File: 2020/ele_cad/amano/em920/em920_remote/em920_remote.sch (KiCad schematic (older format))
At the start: 11 parts, among them SW1 SW_Push, SW2 SW_SPST, U1 ATtiny85-20PU, U2 TY92SS, U3 AE-XCL102D333CR-G

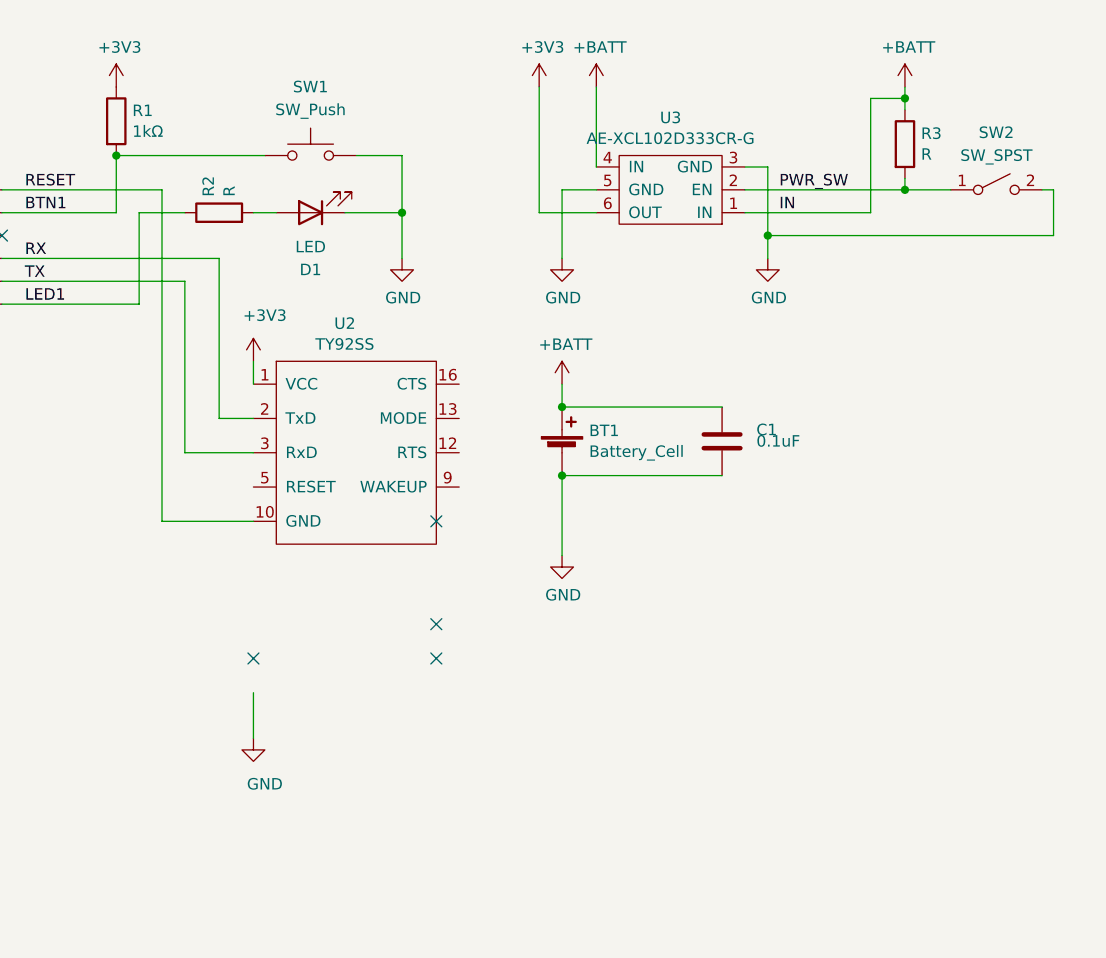
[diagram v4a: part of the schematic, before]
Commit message: リモコンのDCDCを昇降圧に変更
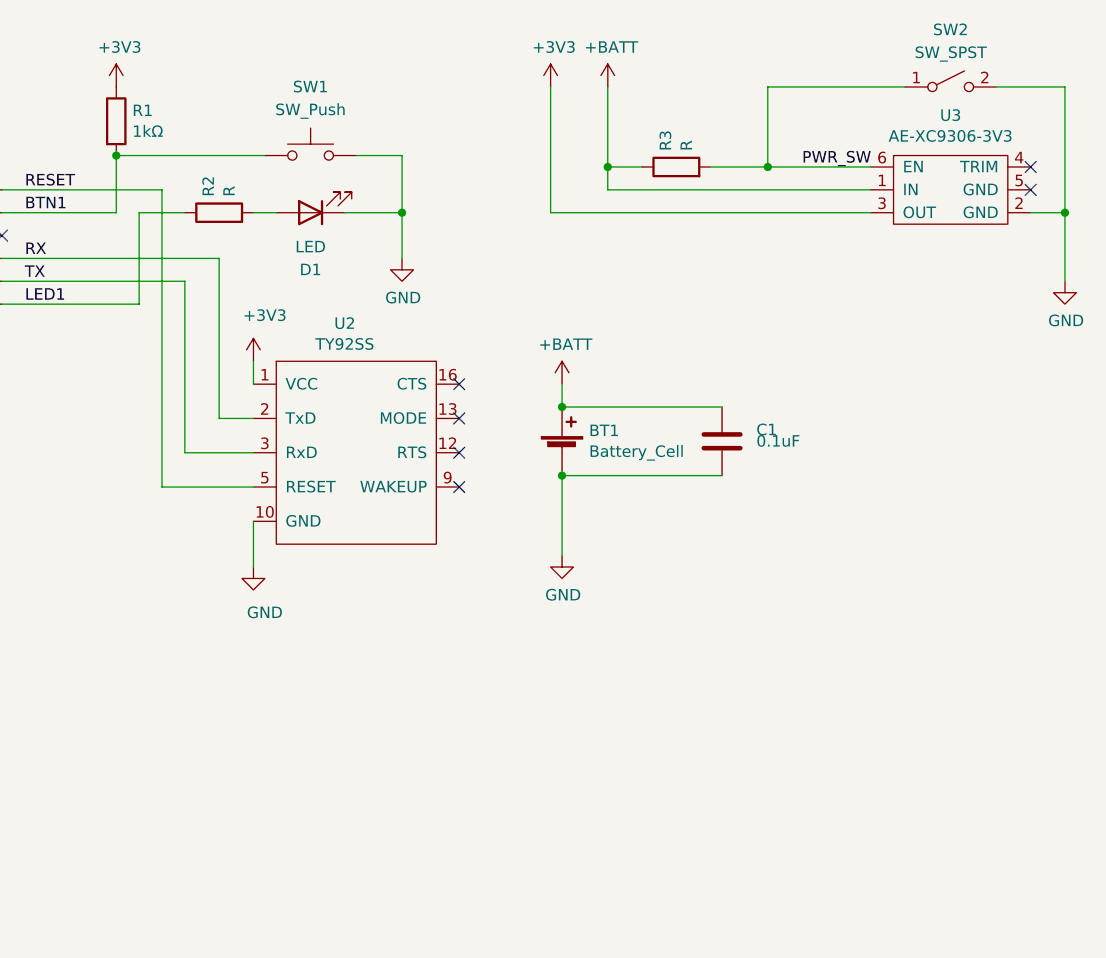
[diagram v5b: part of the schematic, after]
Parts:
- removed U3: AE-XCL102D333CR-G, em920:AE-XCL102D333CR-G, symbol em920:AE-XCL102D333CR-G
- added U3: AE-XC9306-3V3, em920:AE-XC9306-3V3, symbol em920:AE-XC9306-3V3
- BT1: footprint Battery:BatteryHolder_Keystone_103_1x20mm -> Connector_PinHeader_2.54mm:PinHeader_1x03_P2.54mm_Vertical
- R1, R2, R3: footprint Resistor_THT:R_Axial_DIN0207_L6.3mm_D2.5mm_P2.54mm_Vertical -> Resistor_THT:R_Axial_DIN0207_L6.3mm_D2.5mm_P7.62mm_Horizontal
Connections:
- net +3V3: now also U3.3 (OUT)
- net +BATT: now also U3.1 (IN)
- net GND: now also U2.10 (GND), U3.2 (GND)
- net PWR_SW: now also U3.6 (EN)
- net RESET: now also U2.5 (RESET); no longer U2.10 (GND)
- no-connect marks 6 -> 8
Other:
- moved on the sheet: R3, SW2
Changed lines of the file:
@@
 L power:GND #PWR04
 U 1 1 60FD4012
-P 5400 5950
-F 0 "#PWR04" H 5400 5700 50  0001 C CNN
-F 1 "GND" H 5450 5750 50  0000 C CNN
-F 2 "" H 5400 5950 50  0001 C CNN
-F 3 "" H 5400 5950 50  0001 C CNN
-	1    5400 5950
-	1    0    0    -1
-$EndComp
-Wire Wire Line
-	5400 5750 5400 5950
-Wire Wire Line
-	5000 5000 5400 5000
+P 5400 5200
+F 0 "#PWR04" H 5400 4950 50  0001 C CNN
+F 1 "GND" H 5450 5000 50  0000 C CNN
+F 2 "" H 5400 5200 50  0001 C CNN
+F 3 "" H 5400 5200 50  0001 C CNN
+	1    5400 5200
+	1    0    0    -1
+$EndComp
+Wire Wire Line
+	5400 5000 5400 5200
+Wire Wire Line
+	5000 4850 5400 4850
 Text Label 4400 3550 0    50   ~ 0
 RESET
 Wire Wire Line
 	4300 3950 5100 3950
-NoConn ~ 6200 5000
-NoConn ~ 6200 5450
-NoConn ~ 6200 5600
-NoConn ~ 5400 5600
 NoConn ~ 2750 2850
 $Comp
@@
 F 0 "BT1" H 6868 4796 50  0000 L CNN
 F 1 "Battery_Cell" H 6868 4705 50  0000 L CNN
-F 2 "Battery:BatteryHolder_Keystone_103_1x20mm" V 6750 4760 50  0001 C CNN
+F 2 "Connector_PinHeader_2.54mm:PinHeader_1x03_P2.54mm_Vertical" V 6750 4760 50  0001 C CNN
 F 3 "~" V 6750 4760 50  0001 C CNN
 	1    6750 4700
@@
 F 0 "R2" H 5320 3696 50  0000 L CNN
 F 1 "R" H 5320 3605 50  0000 L CNN
-F 2 "Resistor_THT:R_Axial_DIN0207_L6.3mm_D2.5mm_P2.54mm_Vertical" V 5180 3650 50  0001 C CNN
+F 2 "Resistor_THT:R_Axial_DIN0207_L6.3mm_D2.5mm_P7.62mm_Horizontal" V 5180 3650 50  0001 C CNN
 F 3 "~" H 5250 3650 50  0001 C CNN
 	1    5250 3650
@@
 F 0 "R1" H 4870 3296 50  0000 L CNN
 F 1 "1kΩ" H 4870 3205 50  0000 L CNN
-F 2 "Resistor_THT:R_Axial_DIN0207_L6.3mm_D2.5mm_P2.54mm_Vertical" V 4730 3250 50  0001 C CNN
+F 2 "Resistor_THT:R_Axial_DIN0207_L6.3mm_D2.5mm_P7.62mm_Horizontal" V 4730 3250 50  0001 C CNN
 F 3 "~" H 4800 3250 50  0001 C CNN
 	1    4800 3250
@@
 	4300 3550 5000 3550
 Wire Wire Line
-	5000 3550 5000 5000
+	5000 3550 5000 4850
 Wire Wire Line
 	5400 3650 5500 3650
@@
 	4900 3650 5100 3650
 $Comp
-L power:GND #PWR011
-U 1 1 61018775
-P 6750 3850
-F 0 "#PWR011" H 6750 3600 50  0001 C CNN
-F 1 "GND" H 6755 3677 50  0000 C CNN
-F 2 "" H 6750 3850 50  0001 C CNN
-F 3 "" H 6750 3850 50  0001 C CNN
-	1    6750 3850
-	1    0    0    -1
-$EndComp
-$Comp
 L power:+3V3 #PWR012
 U 1 1 6101B33D
-P 6650 3100
-F 0 "#PWR012" H 6650 2950 50  0001 C CNN
-F 1 "+3V3" H 6665 3273 50  0000 C CNN
-F 2 "" H 6650 3100 50  0001 C CNN
-F 3 "" H 6650 3100 50  0001 C CNN
-	1    6650 3100
+P 6700 3100
+F 0 "#PWR012" H 6700 2950 50  0001 C CNN
+F 1 "+3V3" H 6715 3273 50  0000 C CNN
+F 2 "" H 6700 3100 50  0001 C CNN
+F 3 "" H 6700 3100 50  0001 C CNN
+	1    6700 3100
 	1    0    0    -1
 $EndComp
@@
 $EndComp
 $Comp
-L em920:AE-XCL102D333CR-G U3
-U 1 1 6105883F
-P 7550 3450
-F 0 "U3" H 7875 3235 50  0000 C CNN
-F 1 "AE-XCL102D333CR-G" H 7875 3326 50  0000 C CNN
-F 2 "em920:AE-XCL102D333CR-G" H 7850 3750 50  0001 C CNN
-F 3 "" H 7850 3750 50  0001 C CNN
-	1    7550 3450
-	-1   0    0    1
-$EndComp
-Wire Wire Line
-	6900 3100 6900 3450
-$Comp
 L power:+BATT #PWR09
 U 1 1 6101B870
-P 6900 3100
-F 0 "#PWR09" H 6900 2950 50  0001 C CNN
-F 1 "+BATT" H 6915 3273 50  0000 C CNN
-F 2 "" H 6900 3100 50  0001 C CNN
-F 3 "" H 6900 3100 50  0001 C CNN
-	1    6900 3100
-	1    0    0    -1
-$EndComp
-Wire Wire Line
-	6900 3550 6750 3550
-Wire Wire Line
-	6650 3650 6650 3100
-$Comp
-L Switch:SW_SPST SW2
-U 1 1 610E4997
-P 8650 3550
-F 0 "SW2" H 8650 3800 50  0000 C CNN
-F 1 "SW_SPST" H 8650 3700 50  0000 C CNN
-F 2 "em920:SlideSW" H 8650 3550 50  0001 C CNN
-F 3 "~" H 8650 3550 50  0001 C CNN
-	1    8650 3550
-	1    0    0    -1
-$EndComp
-$Comp
-L Device:R R3
-U 1 1 610E7CBC
-P 8250 3350
-F 0 "R3" H 8320 3396 50  0000 L CNN
-F 1 "R" H 8320 3305 50  0000 L CNN
-F 2 "Resistor_THT:R_Axial_DIN0207_L6.3mm_D2.5mm_P2.54mm_Vertical" V 8180 3350 50  0001 C CNN
-F 3 "~" H 8250 3350 50  0001 C CNN
-	1    8250 3350
-	1    0    0    -1
-$EndComp
-$Comp
-L power:+BATT #PWR014
-U 1 1 610EDAF3
-P 8250 3100
-F 0 "#PWR014" H 8250 2950 50  0001 C CNN
-F 1 "+BATT" H 8265 3273 50  0000 C CNN
-F 2 "" H 8250 3100 50  0001 C CNN
-F 3 "" H 8250 3100 50  0001 C CNN
-	1    8250 3100
-	1    0    0    -1
-$EndComp
-Wire Wire Line
-	6750 3550 6750 3850
-$Comp
-L power:GND #PWR013
-U 1 1 610F5EE2
-P 7650 3850
-F 0 "#PWR013" H 7650 3600 50  0001 C CNN
-F 1 "GND" H 7655 3677 50  0000 C CNN
-F 2 "" H 7650 3850 50  0001 C CNN
-F 3 "" H 7650 3850 50  0001 C CNN
-	1    7650 3850
-	1    0    0    -1
-$EndComp
-Wire Wire Line
-	7550 3450 7650 3450
-Wire Wire Line
-	7650 3450 7650 3750
+P 6950 3100
+F 0 "#PWR09" H 6950 2950 50  0001 C CNN
+F 1 "+BATT" H 6965 3273 50  0000 C CNN
+F 2 "" H 6950 3100 50  0001 C CNN
+F 3 "" H 6950 3100 50  0001 C CNN
+	1    6950 3100
+	1    0    0    -1
+$EndComp
+Wire Wire Line
+	6700 3650 6700 3100
 $Comp
 L power:+BATT #PWR0102
@@
 	-1   0    0    1
 $EndComp
-Wire Wire Line
-	6650 3650 6900 3650
-Wire Wire Line
-	7550 3550 8250 3550
-Wire Wire Line
-	8250 3500 8250 3550
-Connection ~ 8250 3550
-Wire Wire Line
-	8250 3100 8250 3150
-Wire Wire Line
-	7550 3650 8100 3650
-Wire Wire Line
-	8100 3650 8100 3150
-Wire Wire Line
-	8100 3150 8250 3150
-Connection ~ 8250 3150
-Wire Wire Line
-	8250 3150 8250 3200
-Connection ~ 7650 3750
-Wire Wire Line
-	7650 3750 7650 3850
-Wire Wire Line
-	8250 3550 8450 3550
-Wire Wire Line
-	8850 3550 8900 3550
-Wire Wire Line
-	8900 3550 8900 3750
-Wire Wire Line
-	7650 3750 8900 3750
-Text Label 7700 3550 0    50   ~ 0
+NoConn ~ 6300 4400
+NoConn ~ 6300 4550
+NoConn ~ 6300 4700
+NoConn ~ 6300 4850
+$Comp
+L Device:R R3
+U 1 1 610E7CBC
+P 7250 3450
+F 0 "R3" H 7320 3496 50  0000 L CNN
+F 1 "R" H 7320 3405 50  0000 L CNN
+F 2 "Resistor_THT:R_Axial_DIN0207_L6.3mm_D2.5mm_P7.62mm_Horizontal" V 7180 3450 50  0001 C CNN
+F 3 "~" H 7250 3450 50  0001 C CNN
+	1    7250 3450
+	0    -1   -1   0
+$EndComp
+Wire Wire Line
+	6950 3100 6950 3450
+$Comp
+L Switch:SW_SPST SW2
+U 1 1 610E4997
+P 8450 3100
+F 0 "SW2" H 8450 3350 50  0000 C CNN
+F 1 "SW_SPST" H 8450 3250 50  0000 C CNN
+F 2 "em920:SlideSW" H 8450 3100 50  0001 C CNN
+F 3 "~" H 8450 3100 50  0001 C CNN
+	1    8450 3100
+	1    0    0    -1
+$EndComp
+$Comp
+L power:GND #PWR011
+U 1 1 61018775
+P 8950 3950
+F 0 "#PWR011" H 8950 3700 50  0001 C CNN
+F 1 "GND" H 8955 3777 50  0000 C CNN
+F 2 "" H 8950 3950 50  0001 C CNN
+F 3 "" H 8950 3950 50  0001 C CNN
+	1    8950 3950
+	1    0    0    -1
+$EndComp
+$Comp
+L em920:AE-XC9306-3V3 U3
+U 1 1 6117DFD8
+P 8450 3350
+F 0 "U3" H 8450 3475 50  0000 C CNN
+F 1 "AE-XC9306-3V3" H 8450 3384 50  0000 C CNN
+F 2 "em920:AE-XC9306-3V3" H 8200 3350 50  0001 C CNN
+F 3 "" H 8200 3350 50  0001 C CNN
+	1    8450 3350
+	1    0    0    -1
+$EndComp
+Wire Wire Line
+	6700 3650 8100 3650
+Wire Wire Line
+	8100 3550 6950 3550
+Text Label 7800 3450 0    50   ~ 0
 PWR_SW
-Text Label 7700 3650 0    50   ~ 0
-IN
+Wire Wire Line
+	7400 3450 7650 3450
+Wire Wire Line
+	7100 3450 6950 3450
+Connection ~ 6950 3450
+Wire Wire Line
+	6950 3450 6950 3550
+Wire Wire Line
+	7650 3450 7650 3100
+Wire Wire Line
+	7650 3100 8250 3100
+Connection ~ 7650 3450
+Wire Wire Line
+	7650 3450 8100 3450
+Wire Wire Line
+	8650 3100 8950 3100
+Wire Wire Line
+	8950 3100 8950 3650
+Wire Wire Line
+	8800 3650 8950 3650
+Connection ~ 8950 3650
+Wire Wire Line
+	8950 3650 8950 3950
+NoConn ~ 8800 3550
+NoConn ~ 8800 3450
 $EndSCHEMATC

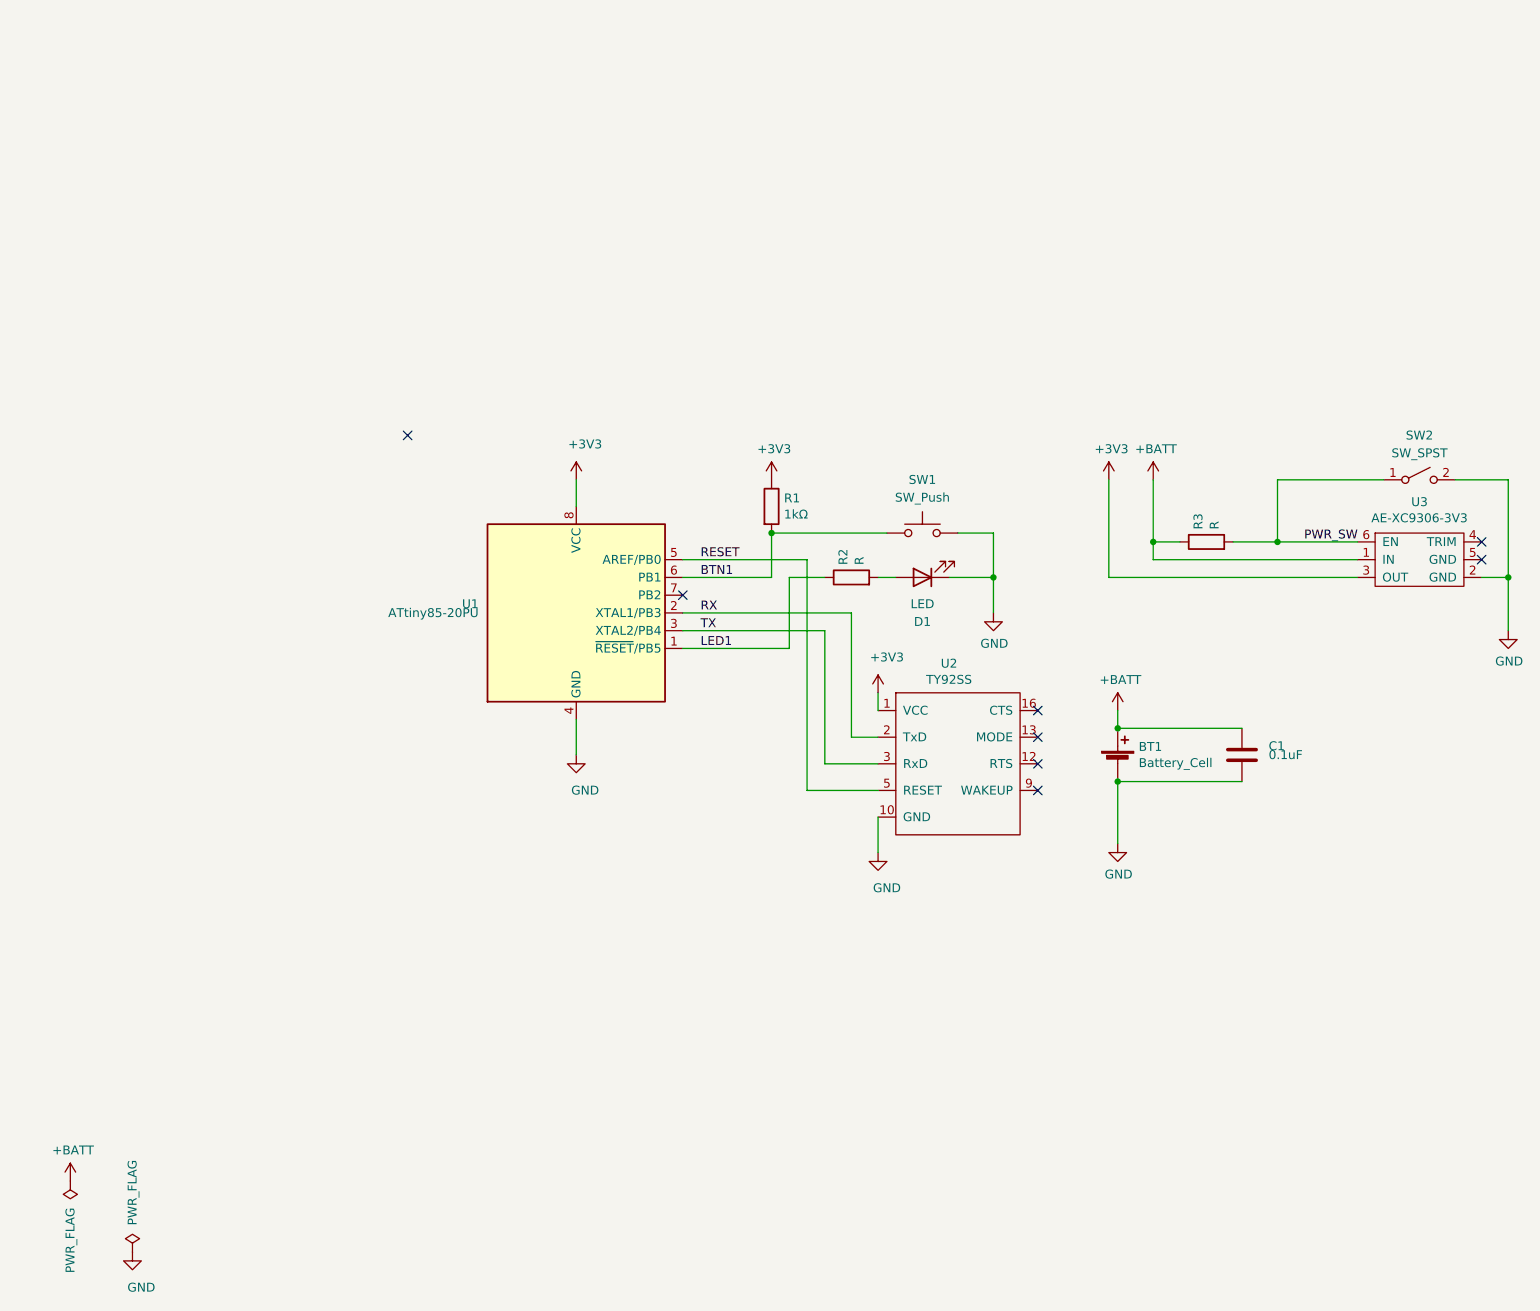
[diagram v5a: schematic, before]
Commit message: 緊急停止リモコンの更新
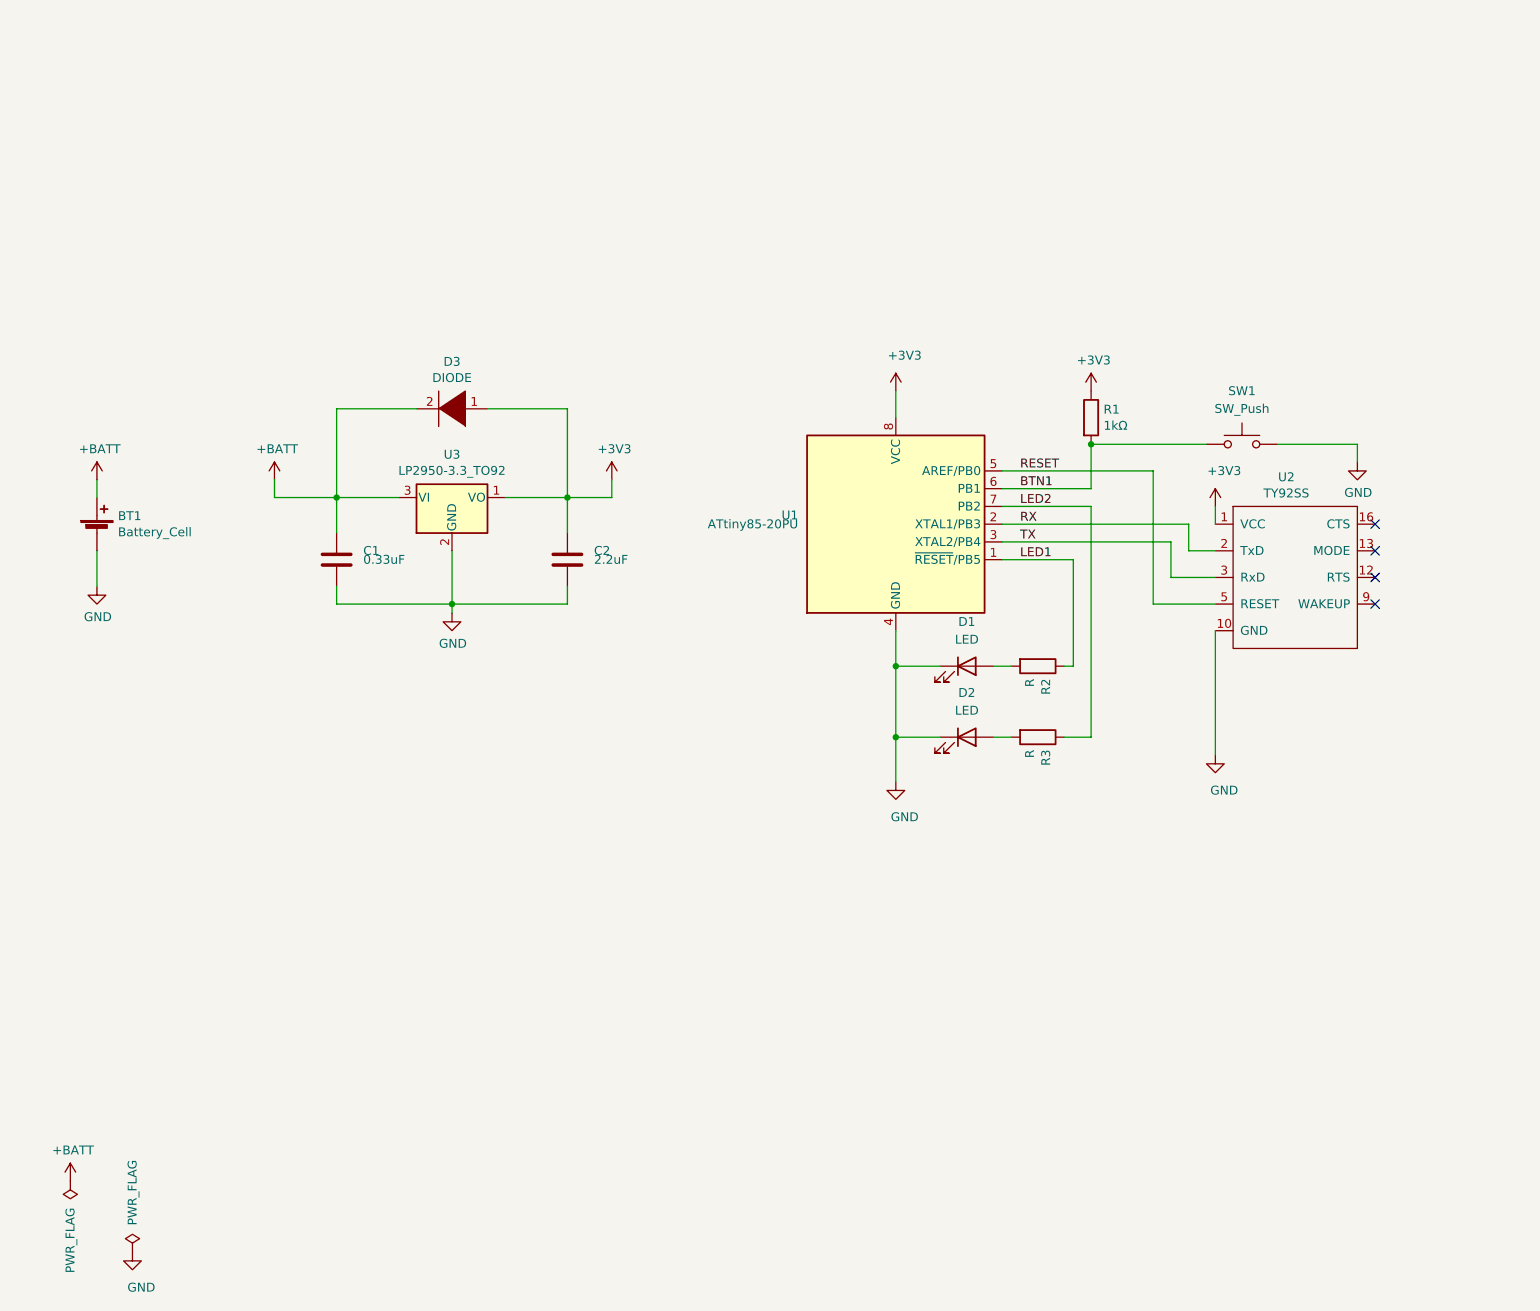
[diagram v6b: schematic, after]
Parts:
- removed SW2: SW_SPST, em920:SlideSW, symbol Switch:SW_SPST
- removed U3: AE-XC9306-3V3, em920:AE-XC9306-3V3, symbol em920:AE-XC9306-3V3
- added C2: 2.2uF, Capacitor_THT:C_Disc_D3.0mm_W1.6mm_P2.50mm, symbol Device:C
- added D2: LED, LED_THT:LED_D3.0mm_FlatTop, symbol Device:LED
- added D3: DIODE, Diode_THT:D_A-405_P7.62mm_Horizontal, symbol pspice:DIODE
- added U3: LP2950-3.3_TO92, Package_TO_SOT_THT:TO-92_Inline_Wide, symbol Regulator_Linear:LP2950-3.3_TO92
- C1: value 0.1uF -> 0.33uF
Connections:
- net +3V3: now also C2.1, D3.1 (K), U3.1 (VO)
- net +BATT: now also D3.2 (A), U3.3 (VI); no longer R3.1
- net GND: now also C2.2, D2.1 (K), U3.2 (GND)
- net LED2: now reaches U1.7 (PB2)
- net LED2: now also R3.1
- net PWR_SW: no longer names the net of R3.2
- net PWR_SW: now also D2.2 (A)
- no-connect marks 8 -> 4
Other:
- moved on the sheet: BT1, C1, D1, R1, R2, SW1, U1, U2
